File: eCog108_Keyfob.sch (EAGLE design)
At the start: 1 part

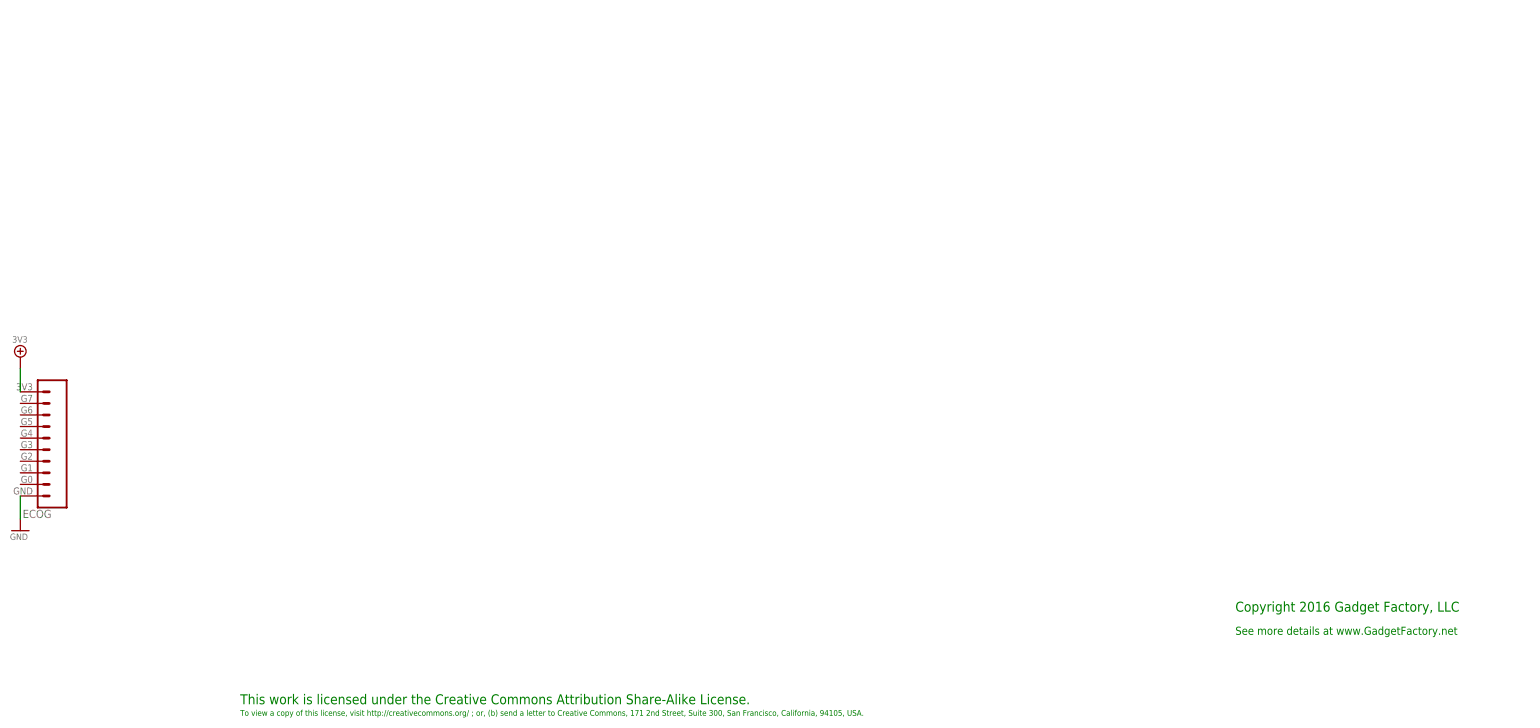
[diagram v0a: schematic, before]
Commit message: Added new eCogs
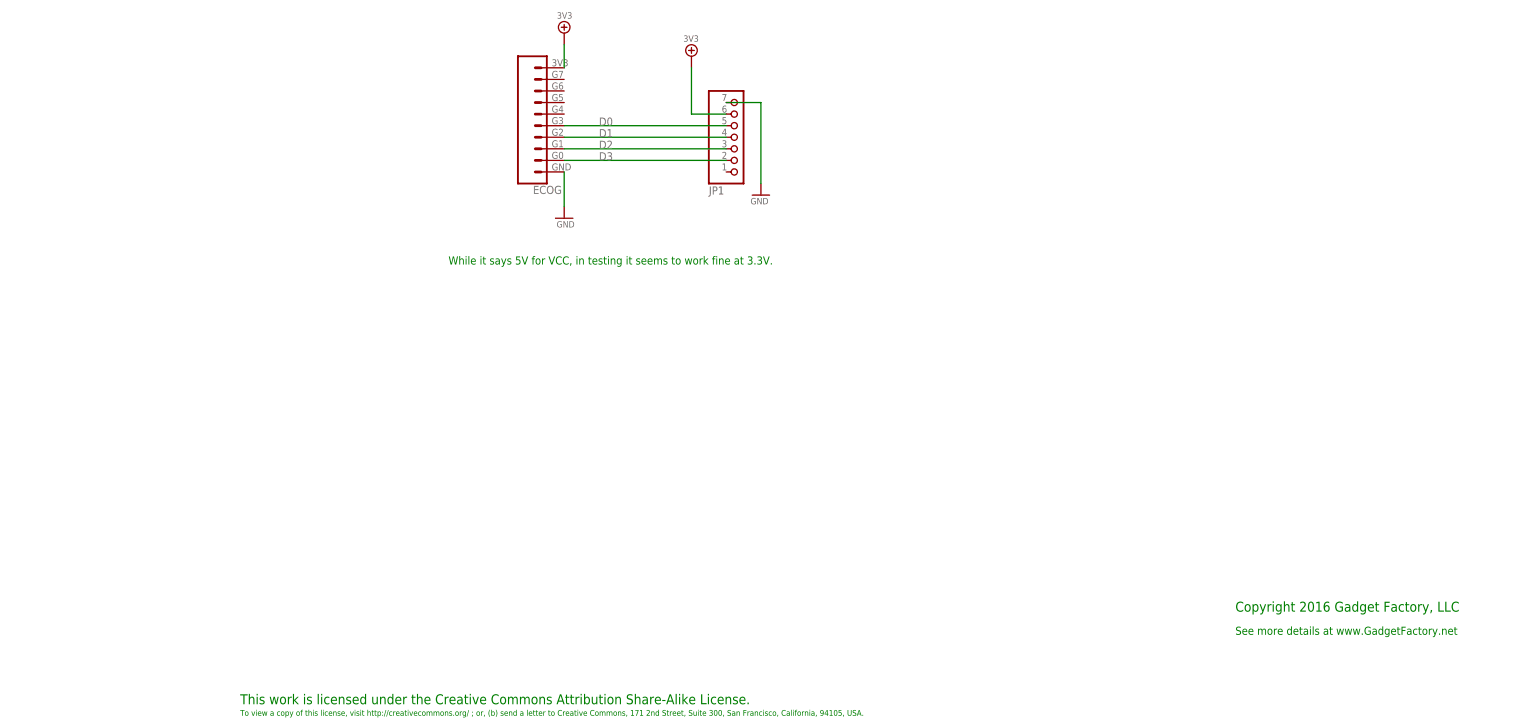
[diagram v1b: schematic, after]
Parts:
- added JP1: (no value), pinhead:PINHD-1X7
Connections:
- new net D0: ECOG.G3, JP1.5
- new net D1: ECOG.G2, JP1.4
- new net D2: ECOG.G1, JP1.3
- new net D3: ECOG.G0, JP1.2
- net 3V3: now also JP1.6
- net GND: now also JP1.7
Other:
- note added: "While it says 5V for VCC, in testing it seems to work fine at 3.3V."
- moved on the sheet: ECOG
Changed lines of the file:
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@@
 <part name="3V3_PWR1" library="eCogs" deviceset="3V3" device=""/>
 <part name="GND1" library="eCogs" deviceset="GND" device=""/>
+<part name="JP1" library="pinhead" deviceset="PINHD-1X7" device=""/>
+<part name="GND2" library="eCogs" deviceset="GND" device=""/>
+<part name="3V3_PWR2" library="eCogs" deviceset="3V3" device=""/>
 </parts>
 <sheets>
@@
 <text x="317.5" y="30.48" size="2.1844" layer="91">Copyright 2016 Gadget Factory, LLC</text>
 <text x="317.5" y="25.4" size="1.778" layer="91">See more details at www.GadgetFactory.net</text>
+<text x="144.78" y="106.68" size="1.778" layer="91">While it says 5V for VCC, in testing it seems to work fine at 3.3V.</text>
 </plain>
 <instances>
 <instance part="FRAME1" gate="G$1" x="0" y="0"/>
-<instance part="ECOG" gate="ECOG_GENERAL" x="55.88" y="53.34"/>
-<instance part="3V3_PWR1" gate="A" x="50.8" y="86.36"/>
-<instance part="GND1" gate="A" x="50.8" y="48.26"/>
+<instance part="ECOG" gate="ECOG_GENERAL" x="165.1" y="124.46" rot="MR0"/>
+<instance part="3V3_PWR1" gate="A" x="170.18" y="157.48" rot="MR0"/>
+<instance part="GND1" gate="A" x="170.18" y="116.84" rot="MR0"/>
+<instance part="JP1" gate="A" x="208.28" y="134.62" rot="MR180"/>
+<instance part="GND2" gate="A" x="213.36" y="121.92"/>
+<instance part="3V3_PWR2" gate="A" x="198.12" y="152.4"/>
 </instances>
 <busses>
@@
 <pinref part="ECOG" gate="ECOG_GENERAL" pin="3V3"/>
 <pinref part="3V3_PWR1" gate="A" pin="3V3"/>
-<wire x1="50.8" y1="83.82" x2="50.8" y2="78.74" width="0.1524" layer="91"/>
+<wire x1="170.18" y1="149.86" x2="170.18" y2="154.94" width="0.2032" layer="91"/>
+</segment>
+<segment>
+<pinref part="3V3_PWR2" gate="A" pin="3V3"/>
+<wire x1="198.12" y1="149.86" x2="198.12" y2="139.7" width="0.2032" layer="91"/>
+<pinref part="JP1" gate="A" pin="6"/>
+<wire x1="198.12" y1="139.7" x2="205.74" y2="139.7" width="0.2032" layer="91"/>
 </segment>
 </net>
@@
 <pinref part="ECOG" gate="ECOG_GENERAL" pin="GND"/>
 <pinref part="GND1" gate="A" pin="GND"/>
-<wire x1="50.8" y1="55.88" x2="50.8" y2="50.8" width="0.2032" layer="91"/>
+<wire x1="170.18" y1="127" x2="170.18" y2="119.38" width="0.2032" layer="91"/>
+</segment>
+<segment>
+<pinref part="JP1" gate="A" pin="7"/>
+<wire x1="205.74" y1="142.24" x2="213.36" y2="142.24" width="0.2032" layer="91"/>
+<pinref part="GND2" gate="A" pin="GND"/>
+<wire x1="213.36" y1="142.24" x2="213.36" y2="124.46" width="0.2032" layer="91"/>
 </segment>
 </net>
+<net name="D3" class="0">
+<segment>
+<pinref part="JP1" gate="A" pin="2"/>
+<pinref part="ECOG" gate="ECOG_GENERAL" pin="G0"/>
+<wire x1="205.74" y1="129.54" x2="170.18" y2="129.54" width="0.2032" layer="91"/>
+<label x="177.8" y="129.54" size="1.778" layer="95"/>
+</segment>
+</net>
+<net name="D2" class="0">
+<segment>
+<pinref part="JP1" gate="A" pin="3"/>
+<pinref part="ECOG" gate="ECOG_GENERAL" pin="G1"/>
+<wire x1="205.74" y1="132.08" x2="170.18" y2="132.08" width="0.2032" layer="91"/>
+<label x="177.8" y="132.08" size="1.778" layer="95"/>
+</segment>
+</net>
+<net name="D1" class="0">
+<segment>
+<pinref part="JP1" gate="A" pin="4"/>
+<pinref part="ECOG" gate="ECOG_GENERAL" pin="G2"/>
+<wire x1="205.74" y1="134.62" x2="170.18" y2="134.62" width="0.2032" layer="91"/>
+<label x="177.8" y="134.62" size="1.778" layer="95"/>
+</segment>
+</net>
+<net name="D0" class="0">
+<segment>
+<pinref part="JP1" gate="A" pin="5"/>
+<pinref part="ECOG" gate="ECOG_GENERAL" pin="G3"/>
+<wire x1="205.74" y1="137.16" x2="170.18" y2="137.16" width="0.2032" layer="91"/>
+<label x="177.8" y="137.16" size="1.778" layer="95"/>
+</segment>
+</net>
